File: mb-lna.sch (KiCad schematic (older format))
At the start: 0 parts

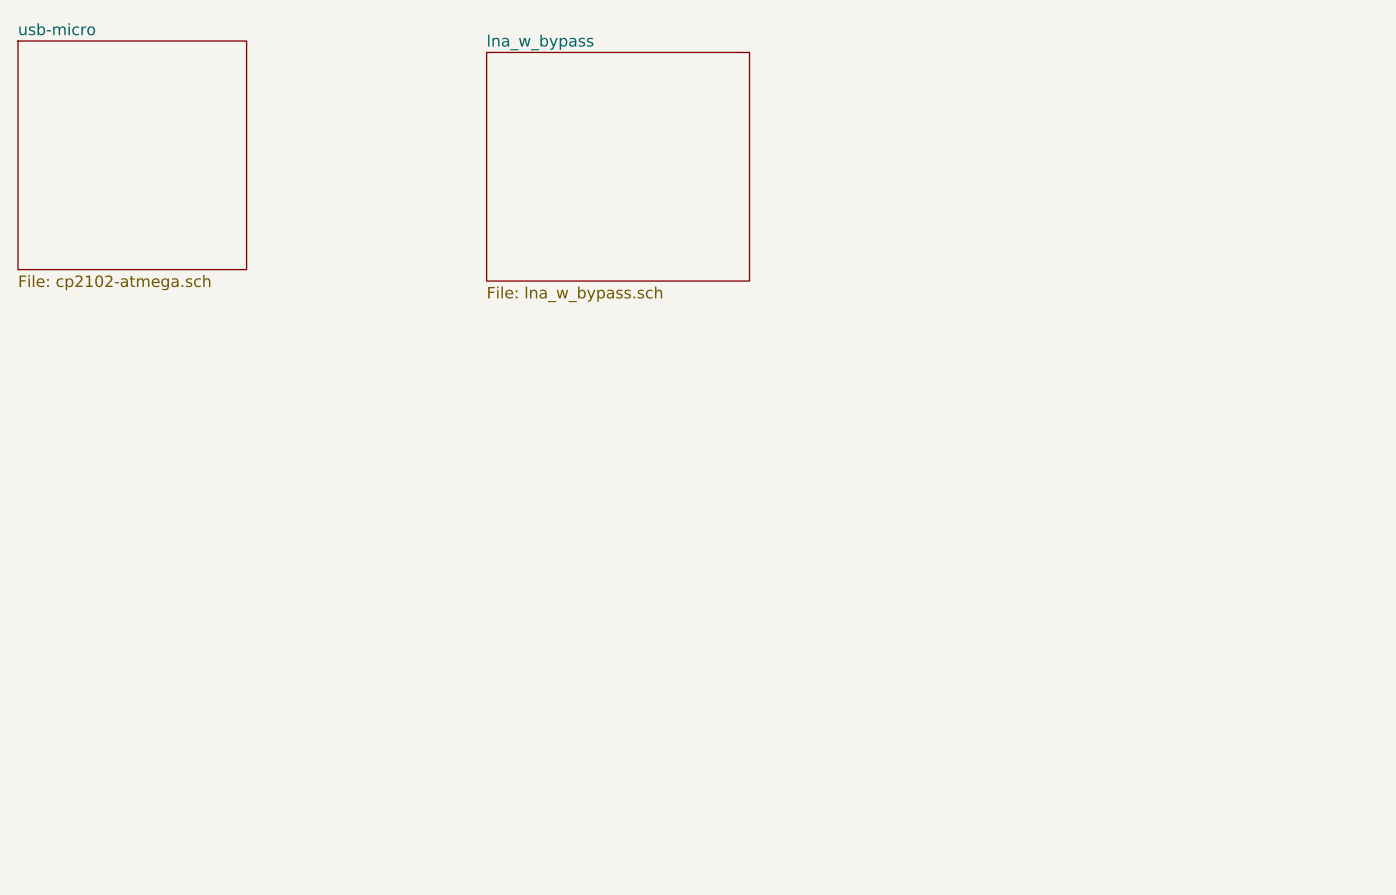
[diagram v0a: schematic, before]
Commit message: Need yet to add the AVR programming connector and the RF filters
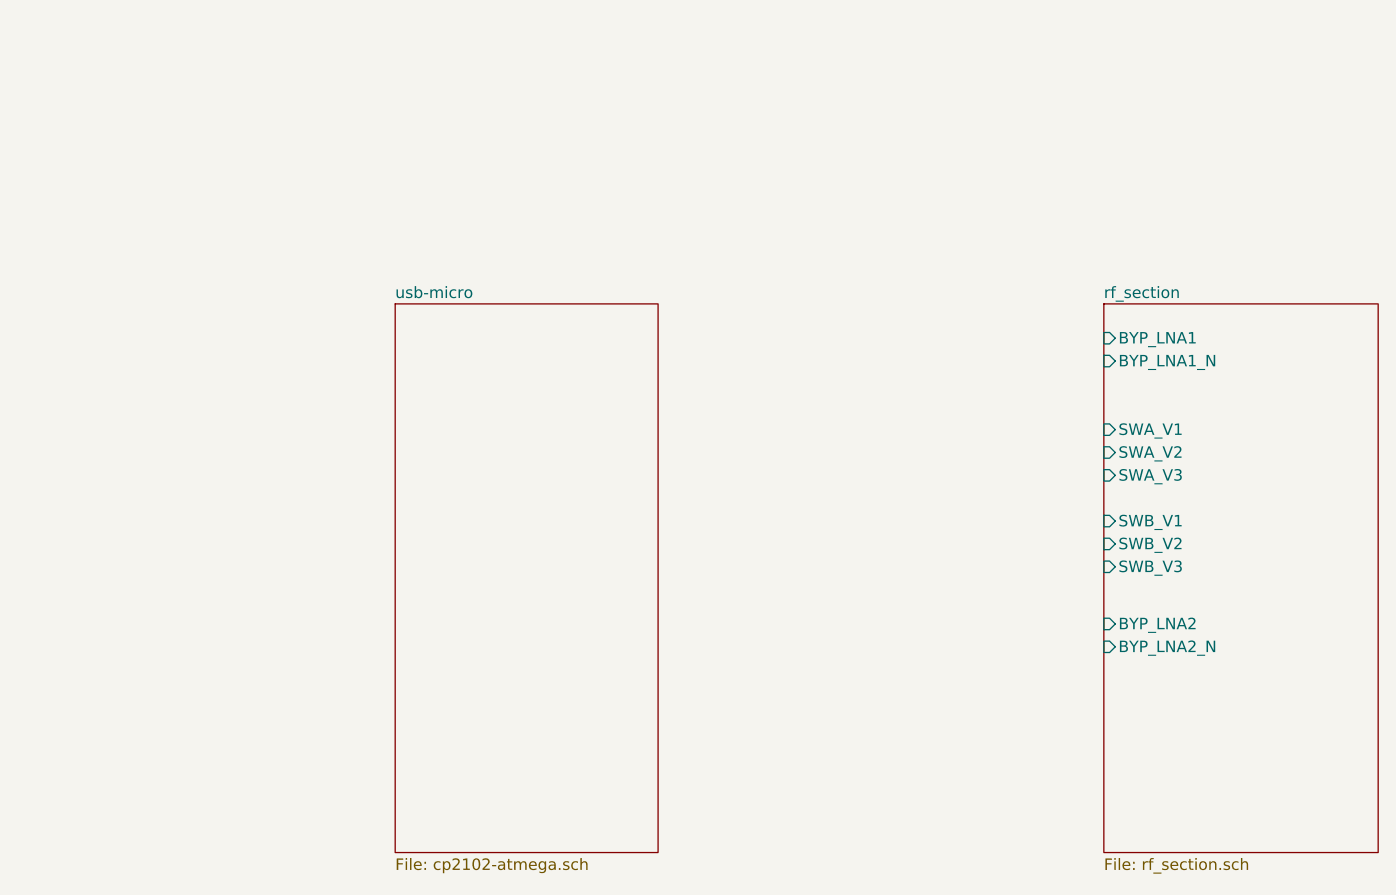
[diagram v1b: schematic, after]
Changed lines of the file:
@@
 $EndDescr
 $Sheet
-S 1500 1500 1000 1000
+S 3150 2650 1150 2400
 U 5B782859
 F0 "usb-micro" 50
@@
 $EndSheet
 $Sheet
-S 3550 1550 1150 1000
+S 6250 2650 1200 2400
 U 5B7DAEA8
-F0 "lna_w_bypass" 50
-F1 "lna_w_bypass.sch" 50
+F0 "rf_section" 50
+F1 "rf_section.sch" 50
+F2 "BYP_LNA1" I L 6250 2800 50
+F3 "BYP_LNA1_N" I L 6250 2900 50
+F4 "SWA_V1" I L 6250 3200 50
+F5 "SWA_V2" I L 6250 3300 50
+F6 "SWA_V3" I L 6250 3400 50
+F7 "SWB_V1" I L 6250 3600 50
+F8 "SWB_V2" I L 6250 3700 50
+F9 "SWB_V3" I L 6250 3800 50
+F10 "BYP_LNA2" I L 6250 4050 50
+F11 "BYP_LNA2_N" I L 6250 4150 50
 $EndSheet
 $EndSCHEMATC

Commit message: Schematic complete. Ready for review.
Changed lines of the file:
@@
 F0 "usb-micro" 50
 F1 "cp2102-atmega.sch" 50
+F2 "BYP_LNA1" O R 4300 2800 50
+F3 "BYP_LNA1_N" O R 4300 2900 50
+F4 "BYP_LNA2" O R 4300 4050 50
+F5 "BYP_LNA2_N" O R 4300 4150 50
+F6 "SWA_V1" O R 4300 3200 50
+F7 "SWA_V2" O R 4300 3300 50
+F8 "SWA_V3" O R 4300 3400 50
+F9 "SWB_V1" O R 4300 3500 50
+F10 "SWB_V2" O R 4300 3600 50
+F11 "SWB_V3" O R 4300 3700 50
 $EndSheet
 $Sheet
@@
 F5 "SWA_V2" I L 6250 3300 50
 F6 "SWA_V3" I L 6250 3400 50
-F7 "SWB_V1" I L 6250 3600 50
-F8 "SWB_V2" I L 6250 3700 50
-F9 "SWB_V3" I L 6250 3800 50
+F7 "SWB_V1" I L 6250 3500 50
+F8 "SWB_V2" I L 6250 3600 50
+F9 "SWB_V3" I L 6250 3700 50
 F10 "BYP_LNA2" I L 6250 4050 50
 F11 "BYP_LNA2_N" I L 6250 4150 50
 $EndSheet
+Wire Wire Line
+	4300 2800 6250 2800
+Wire Wire Line
+	6250 2900 4300 2900
+Wire Wire Line
+	4300 3200 6250 3200
+Wire Wire Line
+	6250 3300 4300 3300
+Wire Wire Line
+	4300 3400 6250 3400
+Wire Wire Line
+	4300 3500 6250 3500
+Wire Wire Line
+	6250 3600 4300 3600
+Wire Wire Line
+	4300 3700 6250 3700
+Wire Wire Line
+	4300 4050 6250 4050
+Wire Wire Line
+	6250 4150 4300 4150
 $EndSCHEMATC
